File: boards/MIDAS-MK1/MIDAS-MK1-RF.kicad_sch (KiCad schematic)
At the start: 16 parts, among them IC401 TESEO-LIV3F, J401 Conn_Coaxial, J402 Conn_Coaxial, U401 RFM96W-433S2, U402 BGA725L6E6327FTSA1

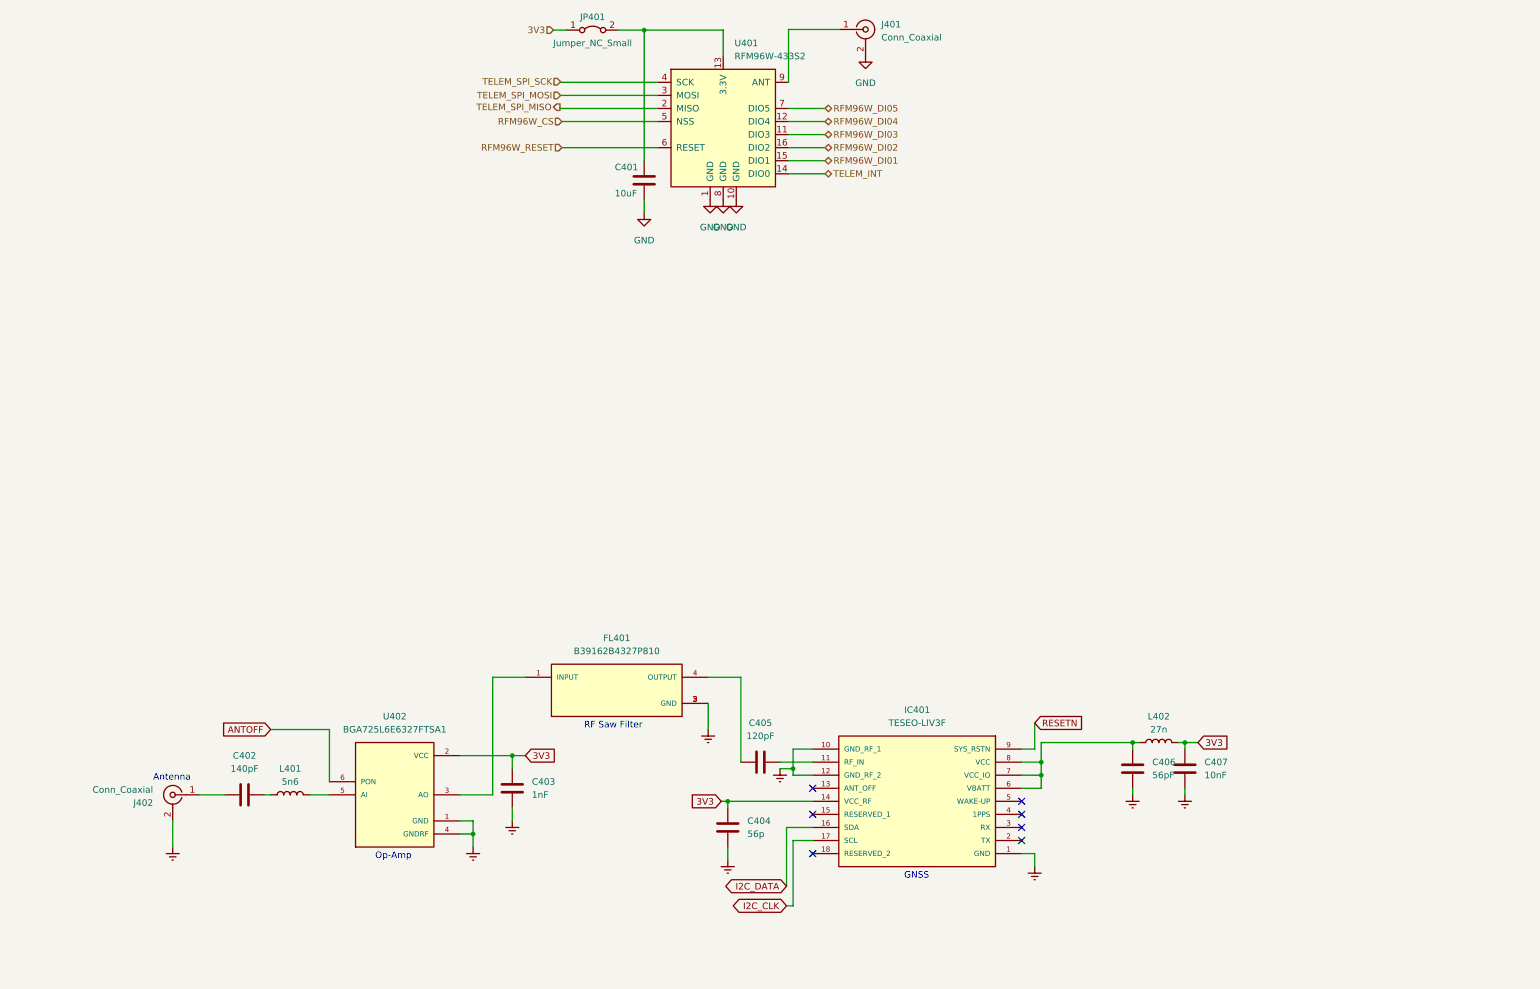
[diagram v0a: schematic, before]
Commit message: Reformat LIV3F Schematic
looks nice
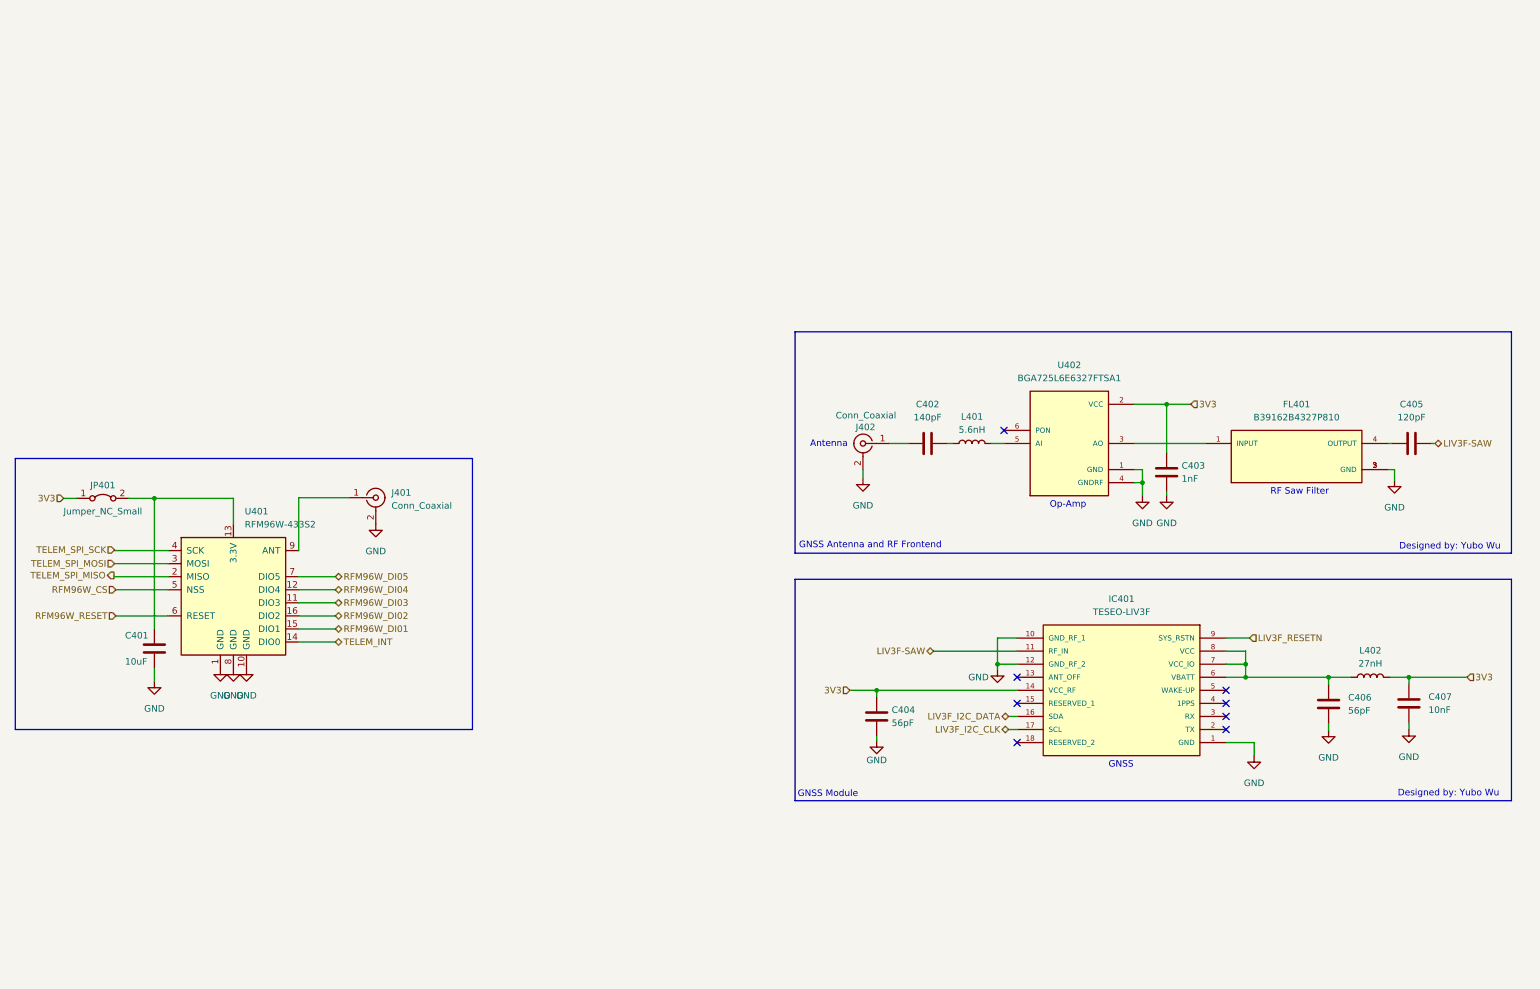
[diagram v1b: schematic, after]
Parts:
- C404: value 56p -> 56pF
- L401: value 5n6 -> 5.6nH
- L402: value 27n -> 27nH
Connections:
- net Earth is gone; now on net GND: C403.1, C404.2, C406.2, C407.2, FL401.2 (GND), FL401.3 (GND), FL401.5 (GND), IC401.10 (GND_RF_1), IC401.12 (GND_RF_2), J402.2 (Ext), U402.1 (GND), U402.4 (GNDRF)
- net GNDREF is gone; now on net GND: IC401.1 (GND)
- net LIV3F-SAW: now reaches C405.2, IC401.11 (RF_IN)
- net ANTOFF: no longer names the net of U402.6 (PON)
- net I2C_CLK renamed LIV3F_I2C_CLK
- net I2C_DATA renamed LIV3F_I2C_DATA
- net RESETN renamed LIV3F_RESETN
- no-connect marks 7 -> 8
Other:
- note added: "Designed by: Yubo Wu"
- note added: "GNSS Antenna and RF Frontend"
- note added: "GNSS Module"
- moved on the sheet: C401, C402, C403, C404, C405, C406, C407, FL401, IC401, J401, J402, JP401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

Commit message: Updated HOPE schematic
Updated HOPE schematic
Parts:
- C401: footprint Capacitor_SMD:C_0805_2012Metric -> Capacitor_SMD:C_0603_1608Metric
- J401: footprint (none) -> Connector_Coaxial:SMA_Amphenol_901-143_Horizontal
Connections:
- net TELEM_INT renamed RFM96W_INT
- net TELEM_SPI_MISO renamed SNS_SPI_MISO
- net TELEM_SPI_MOSI renamed SNS_SPI_MOSI
- net TELEM_SPI_SCK renamed SNS_SPI_SCK
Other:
- moved on the sheet: C401, J401

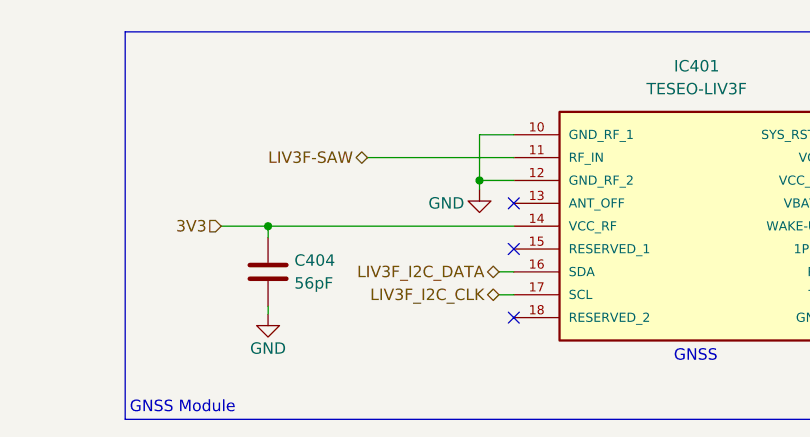
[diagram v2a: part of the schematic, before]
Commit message: Updated I2C data naming convention
Updated I2C data naming convention
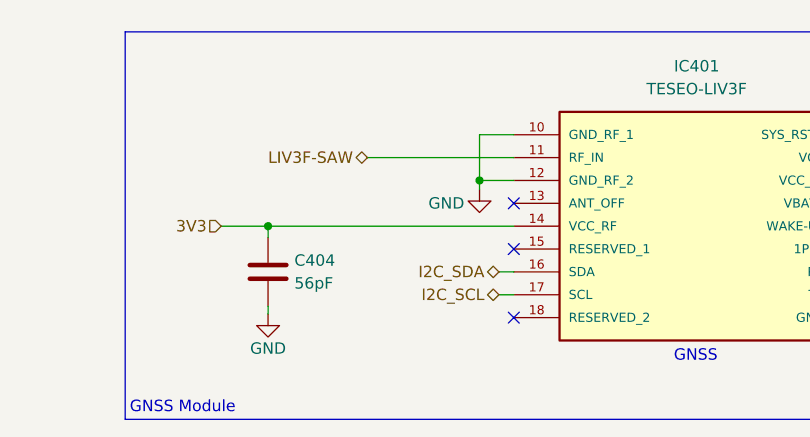
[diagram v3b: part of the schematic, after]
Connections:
- net LIV3F_I2C_CLK renamed I2C_SCL
- net LIV3F_I2C_DATA renamed I2C_SDA

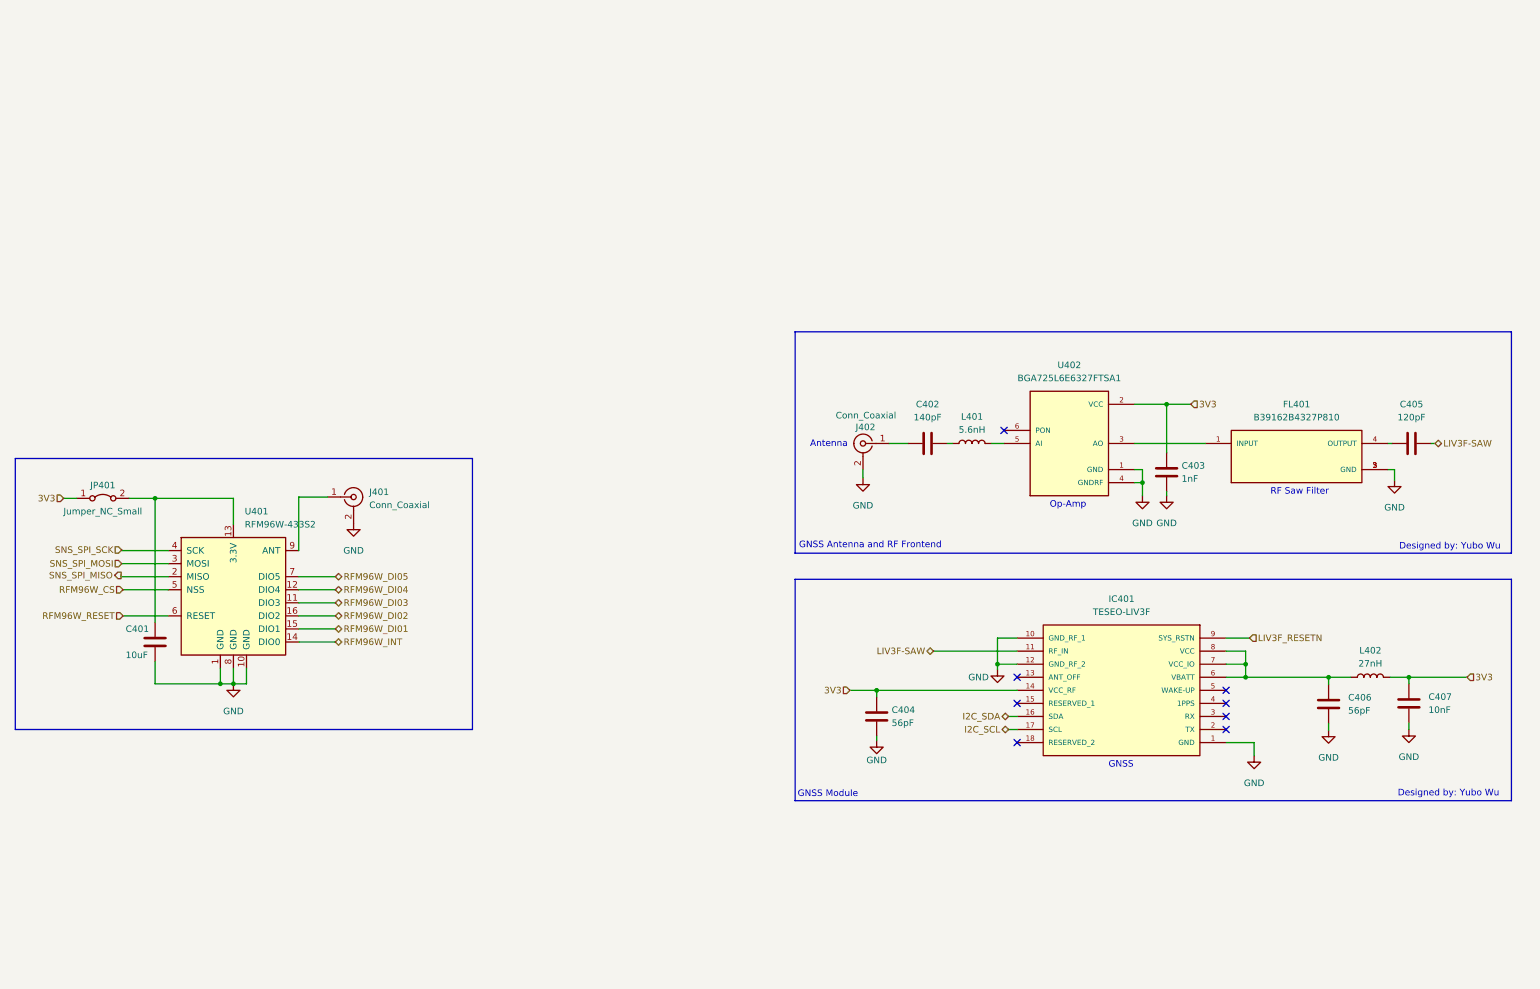
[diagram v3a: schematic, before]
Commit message: updated passive footprints
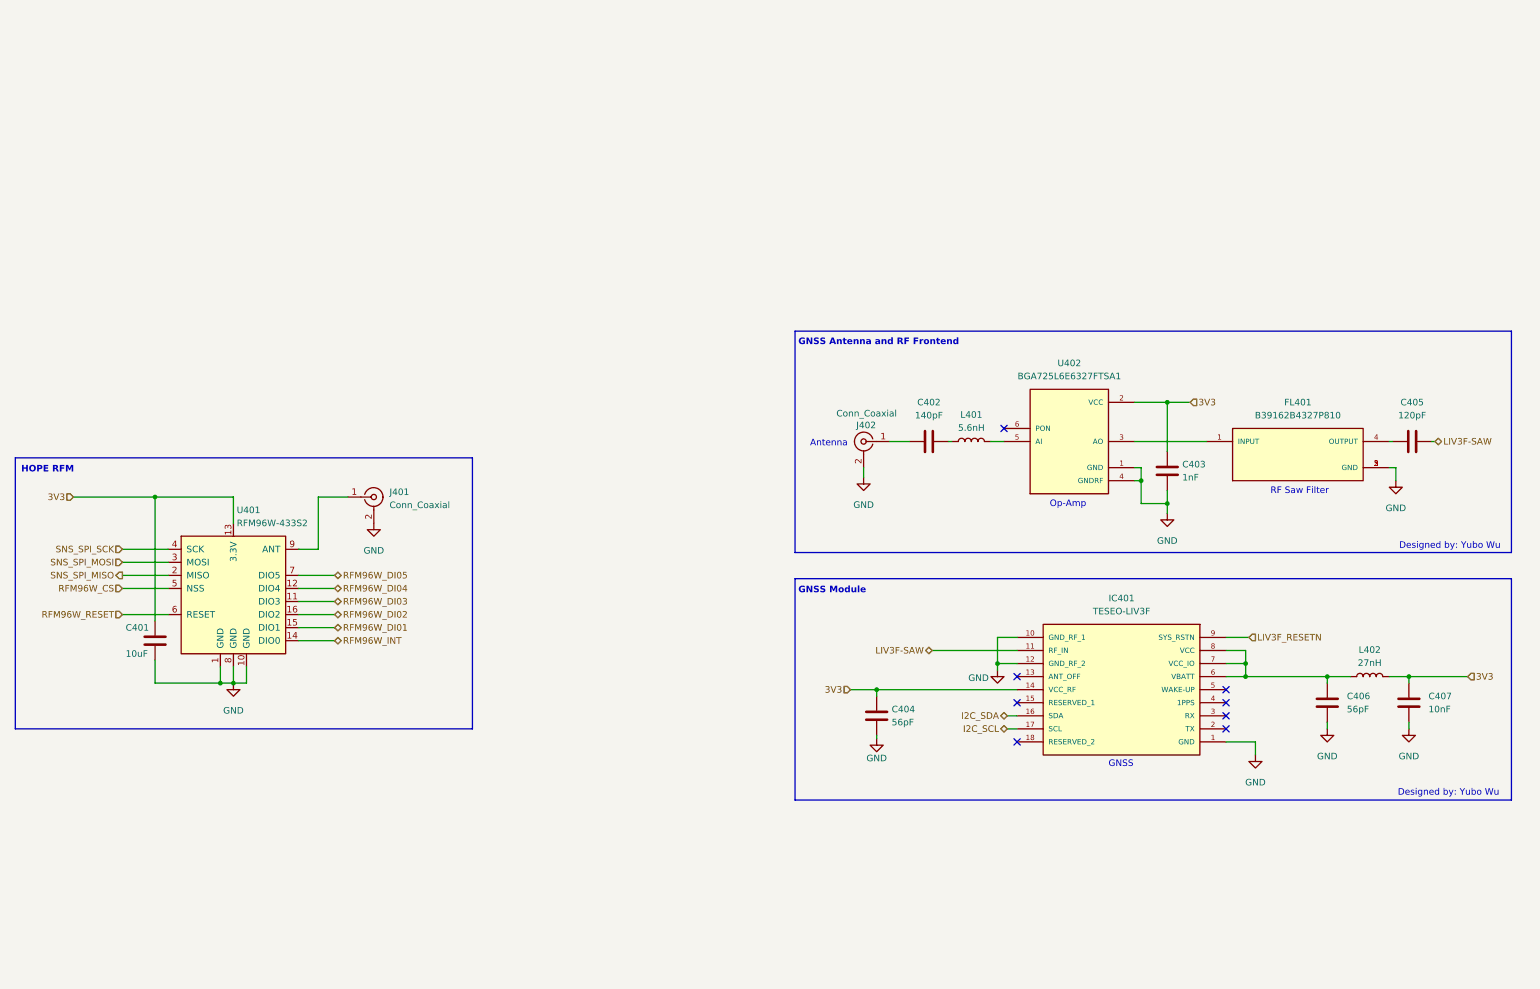
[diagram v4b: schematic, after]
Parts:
- removed JP401: Jumper_NC_Small, Jumper:SolderJumper-2_P1.3mm_Bridged_RoundedPad1.0x1.5mm, symbol Jumper:Jumper_2_Bridged
- C402, C403, C404, C405, C406, C407: footprint Capacitor_SMD:C_0603_1608Metric_Pad1.08x0.95mm_HandSolder -> Capacitor_SMD:C_0603_1608Metric
- L401, L402: footprint Inductor_SMD:L_0603_1608Metric_Pad1.05x0.95mm_HandSolder -> Inductor_SMD:L_0603_1608Metric
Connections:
- net 3V3: now also C401.1, U401.13 (3.3V)
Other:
- note added: "HOPE RFM"
- moved on the sheet: J401

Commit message: added comments
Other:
- note added: "Add part number"
- note added: "Decrease width"

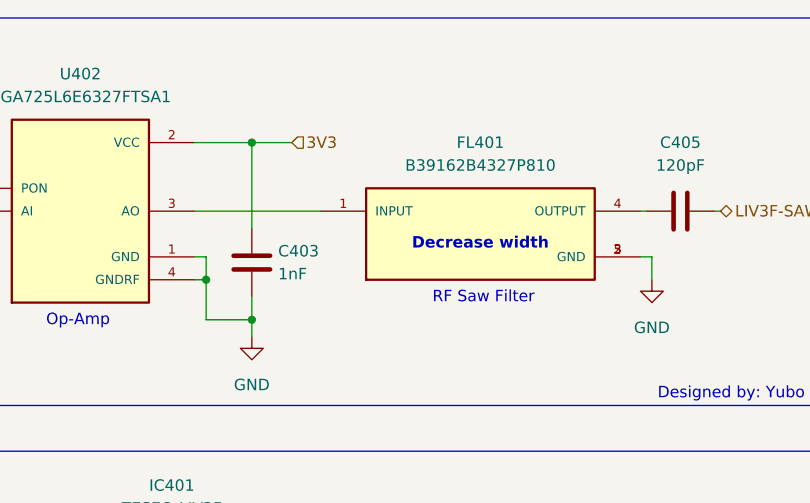
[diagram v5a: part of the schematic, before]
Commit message: made saw filter smaller
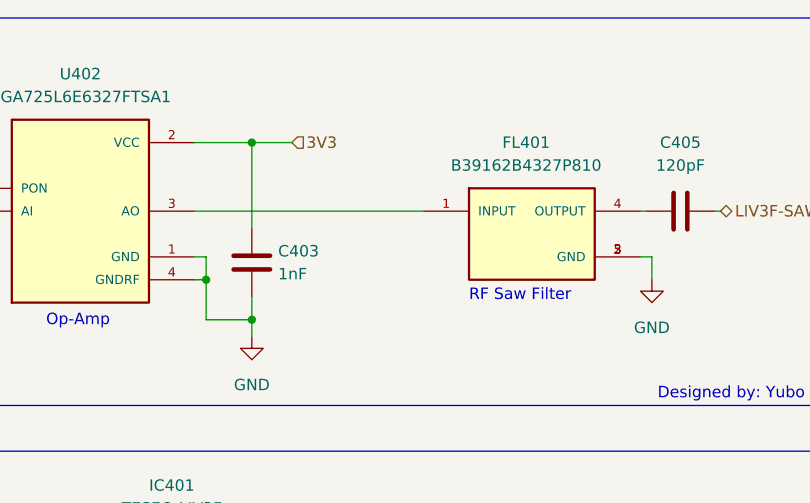
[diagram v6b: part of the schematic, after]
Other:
- note removed: "Decrease width"
- moved on the sheet: FL401

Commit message: general improvements
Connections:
- net LIV3F_RESETN renamed LIV3F_RESET
